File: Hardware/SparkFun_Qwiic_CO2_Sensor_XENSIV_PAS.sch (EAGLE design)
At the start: 41 parts, among them J1 QWIIC_RA, J2 QWIIC_RA, U1 PASCO2V01BUMA1, U2 LMR62421

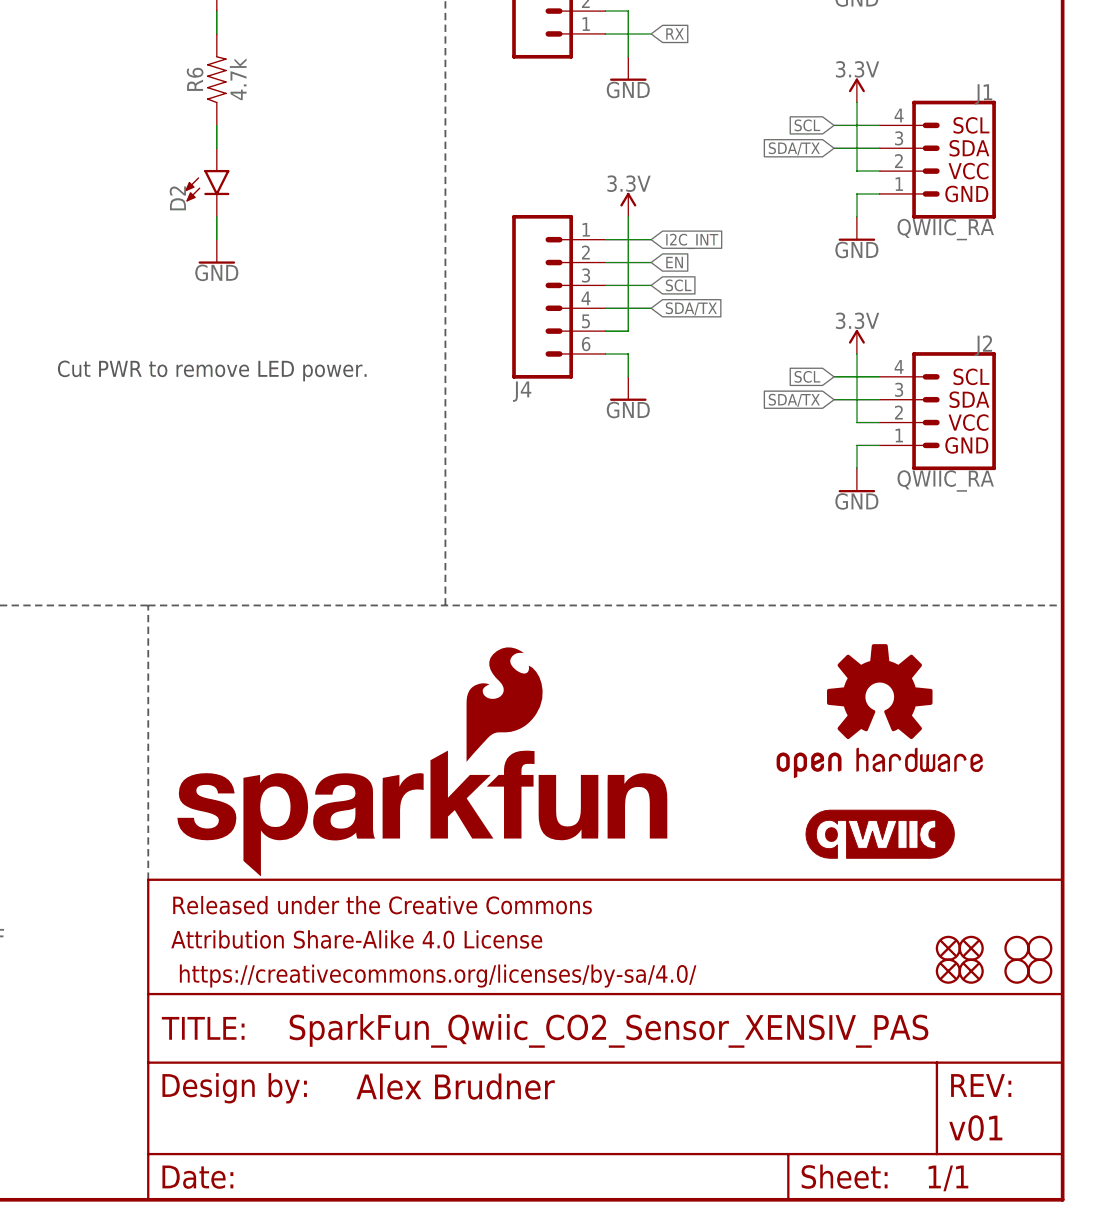
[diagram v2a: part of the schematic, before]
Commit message: Update for v10.
Schematic - Make version v10.
Board - Make version v10. Change size of Silk title text.
Production - Removed individual board gerbers, add panel gerbers.
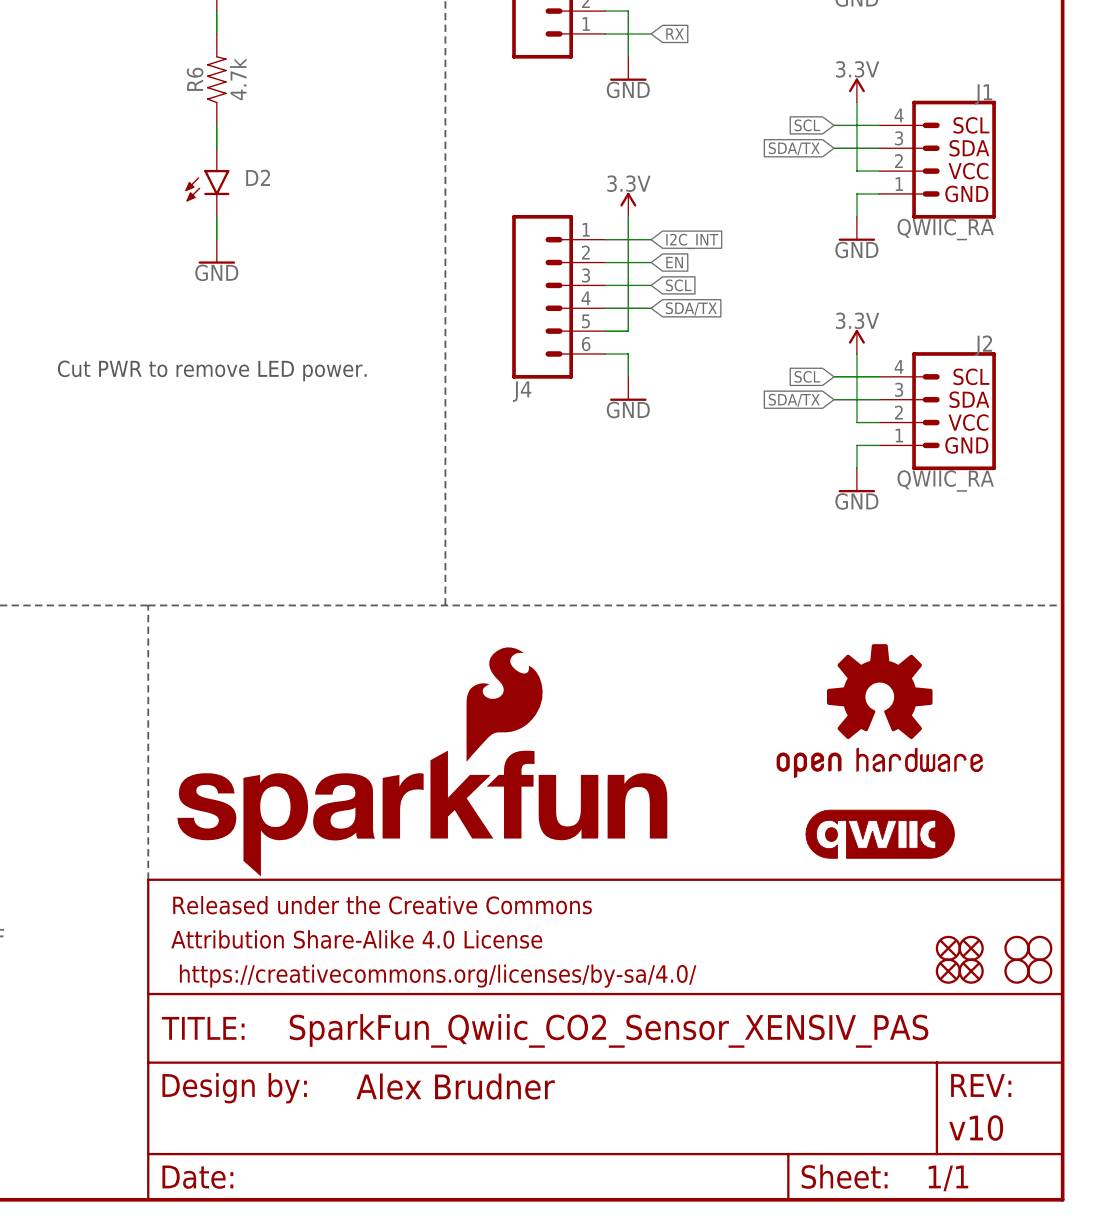
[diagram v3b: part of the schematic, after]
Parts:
- FRAME1: REV v01 -> v10
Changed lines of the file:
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@@
 <part name="FRAME1" library="SparkFun-Aesthetics" deviceset="FRAME-LETTER" device="">
 <attribute name="DESIGNER" value="Alex Brudner"/>
-<attribute name="REV" value="v01"/>
+<attribute name="REV" value="v10"/>
 </part>
 <part name="U1" library="xensiv_pas" deviceset="PASCO2V01" device="" value="PASCO2V01BUMA1"/>
@@
 </instance>
 <instance part="D2" gate="G$1" x="154.94" y="114.3" smashed="yes">
-<attribute name="NAME" x="151.511" y="109.728" size="1.778" layer="95" font="vector" rot="R90"/>
+<attribute name="NAME" x="157.988" y="112.649" size="1.778" layer="95" font="vector"/>
 <attribute name="VALUE" x="156.845" y="109.728" size="1.778" layer="96" font="vector" rot="R90" align="top-left"/>
 </instance>

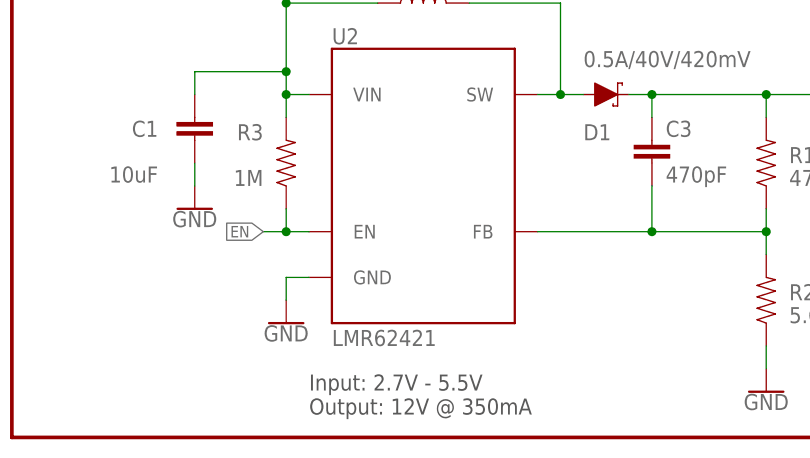
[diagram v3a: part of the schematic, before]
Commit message: BOM change and add logo to silk.
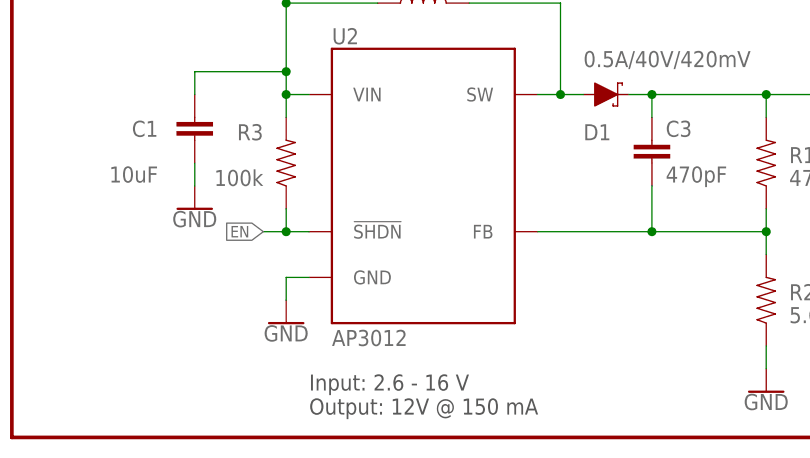
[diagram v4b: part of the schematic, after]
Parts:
- R3: value 1M -> 100k; device SparkFun-Resistors:1MOHM-0603-1/4W-5% -> SparkFun-Resistors:100KOHM-0603-1/10W-1%
- U2: value LMR62421 -> AP3012; device xensiv_pas:LMR62421 -> xensiv_pas:AP3012; PN (none) -> AP3012
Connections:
- net EN: now also U2.!SHDN!; no longer U2.EN
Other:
- note added: "Input: 2.6 - 16 V Output: 12V @ 150 mA"
- note removed: "Input: 2.7V - 5.5V Output: 12V @ 350mA"
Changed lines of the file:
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@@
 <part name="J1" library="SparkFun-Connectors" deviceset="QWIIC_CONNECTOR" device="JS-1MM" value="QWIIC_RA"/>
 <part name="J2" library="SparkFun-Connectors" deviceset="QWIIC_CONNECTOR" device="JS-1MM" value="QWIIC_RA"/>
-<part name="U2" library="xensiv_pas" deviceset="LMR62421" device="" package3d_urn="urn:adsk.eagle:package:40937508/1" value="LMR62421"/>
+<part name="U2" library="xensiv_pas" deviceset="AP3012" device="" package3d_urn="urn:adsk.eagle:package:40937508/1" value="AP3012">
+<attribute name="PN" value="AP3012"/>
+</part>
 <part name="C1" library="SparkFun-Capacitors" deviceset="10UF" device="-0805-25V-10%" value="10uF"/>
 <part name="C2" library="SparkFun-Capacitors" deviceset="4.7UF" device="-0603-35V-(20%)" value="4.7uF"/>
@@
 <part name="R2" library="SparkFun-Resistors" deviceset="5.62KOHM" device="-0603-1/10W-1%" value="5.62k"/>
 <part name="D1" library="SparkFun-DiscreteSemi" deviceset="DIODE-SCHOTTKY" device="-PMEG4005EJ" value="0.5A/40V/420mV"/>
-<part name="R3" library="SparkFun-Resistors" deviceset="1MOHM" device="-0603-1/4W-5%" value="1M"/>
+<part name="R3" library="SparkFun-Resistors" deviceset="100KOHM" device="-0603-1/10W-1%" value="100k"/>
 <part name="GND1" library="SparkFun-PowerSymbols" deviceset="GND" device=""/>
 <part name="GND2" library="SparkFun-PowerSymbols" deviceset="GND" device=""/>
@@
 <wire x1="147.32" y1="35.56" x2="147.32" y2="66.04" width="0.2032" layer="97" style="longdash"/>
 <text x="137.16" y="91.44" size="1.778" layer="97" font="vector">Cut PWR to remove LED power.</text>
-<text x="33.02" y="2.54" size="1.778" layer="97" font="vector">Input: 2.7V - 5.5V
-Output: 12V @ 350mA</text>
+<text x="33.02" y="2.54" size="1.778" layer="97" font="vector">Input: 2.6 - 16 V
+Output: 12V @ 150 mA</text>
 <text x="48.26" y="96.52" size="1.778" layer="97" font="vector">7-bit unshifted address: 0x28</text>
 <text x="53.34" y="81.28" size="1.778" layer="97" font="vector">Power requirements:
@@
 <instance part="U2" gate="G$1" x="45.72" y="27.94" smashed="yes">
 <attribute name="NAME" x="35.56" y="43.688" size="1.778" layer="95" font="vector"/>
-<attribute name="VALUE" x="35.56" y="10.16" size="1.778" layer="96" font="vector"/>
+<attribute name="PN" x="35.56" y="10.16" size="1.778" layer="96" font="vector"/>
 </instance>
 <instance part="C1" gate="G$1" x="20.32" y="33.02" smashed="yes">
@@
 <segment>
 <pinref part="R3" gate="G$1" pin="1"/>
-<pinref part="U2" gate="G$1" pin="EN"/>
+<pinref part="U2" gate="G$1" pin="!SHDN!"/>
 <wire x1="30.48" y1="25.4" x2="30.48" y2="22.86" width="0.1524" layer="91"/>
 <wire x1="30.48" y1="22.86" x2="33.02" y2="22.86" width="0.1524" layer="91"/>
